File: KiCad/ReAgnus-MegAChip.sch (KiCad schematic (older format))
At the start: 24 parts, among them J3 Conn_02x01, J4 Conn_01x01, J5 Conn_01x01, J6 Conn_01x01, J7 Conn_01x01, U1 PLCC-84-Plug, U2 LM1117-3.3, U3 SN74CBTD16210, U4 SN74CBTD16210, U5 SN74CBTD16210, U6 SN74CBTD16210, U8 74LVC1G07, U9 Agnus_TH_plug_pins

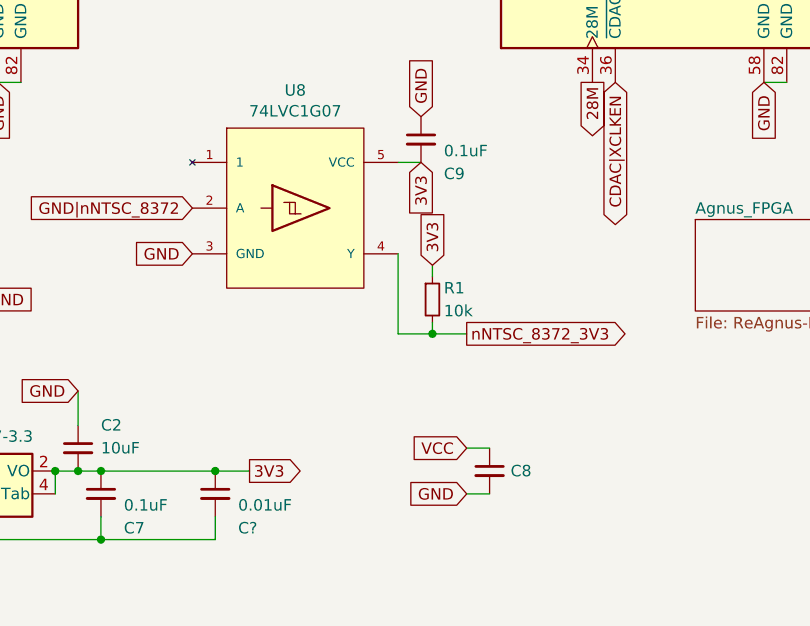
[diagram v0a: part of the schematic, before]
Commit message: fixed routing for VCC to voltage regulator, placed two-pin header for VCC/GND and more routing
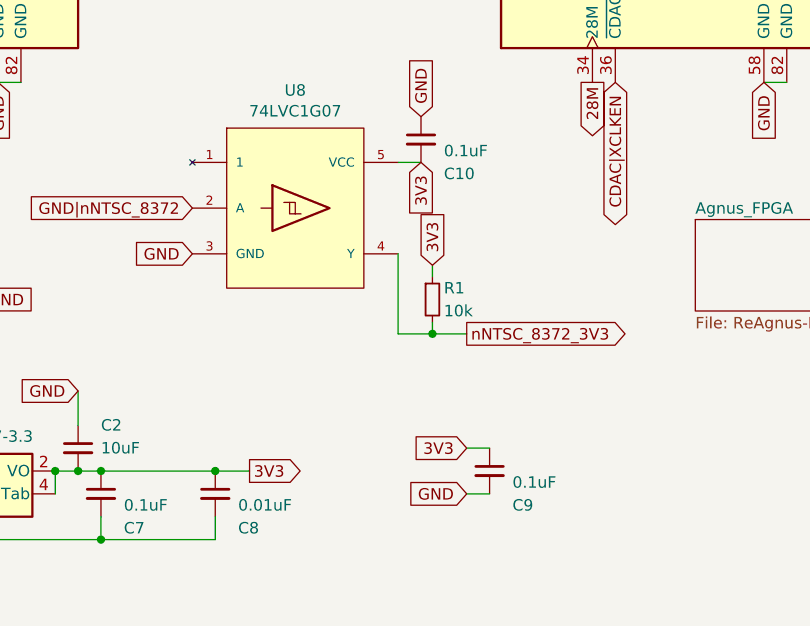
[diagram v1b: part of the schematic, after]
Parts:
- removed C8: C_Small, Capacitor_SMD:C_1210_3225Metric_Pad1.42x2.65mm_HandSolder, symbol Device:C_Small
- added C9: 0.1uF, Capacitor_SMD:C_0805_2012Metric_Pad1.15x1.40mm_HandSolder, symbol Device:C_Small
- gave numbers to parts that had none: 1
- renumbered C9 to C10
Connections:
- net 3V3: now also C9.1
- net GND: now also C9.2
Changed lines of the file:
@@
 GND
 $Comp
-L Device:C_Small C9
+L Device:C_Small C10
 U 1 1 631B6BE4
 P 4150 5950
-AR Path="/631B6BE4" Ref="C9"  Part="1"
+AR Path="/631B6BE4" Ref="C10"  Part="1"
 AR Path="/632D3BDF/631B6BE4" Ref="C?"  Part="1"
 AR Path="/632F104D/631B6BE4" Ref="C?"  Part="1"
-F 0 "C9" H 4250 5800 50  0000 L CNN
+F 0 "C10" H 4250 5800 50  0000 L CNN
 F 1 "0.1uF" H 4250 5900 50  0000 L CNN
 F 2 "Capacitor_SMD:C_0805_2012Metric_Pad1.15x1.40mm_HandSolder" H 4150 5950 50  0001 C CNN
@@
 GND|nNTSC_8372
 Connection ~ 2750 7400
-Text GLabel 4350 7300 0    50   Input ~ 0
-VCC
 Text GLabel 4350 7500 0    50   Input ~ 0
 GND
-$Comp
-L Device:C_Small C8
-U 1 1 631ACF4A
-P 4450 7400
-AR Path="/631ACF4A" Ref="C8"  Part="1"
-AR Path="/632D3BDF/631ACF4A" Ref="C?"  Part="1"
-AR Path="/632F104D/631ACF4A" Ref="C?"  Part="1"
-F 0 "C8" H 4542 7400 50  0000 L CNN
-F 1 "C_Small" H 4542 7355 50  0001 L CNN
-F 2 "Capacitor_SMD:C_1210_3225Metric_Pad1.42x2.65mm_HandSolder" H 4450 7400 50  0001 C CNN
-F 3 "~" H 4450 7400 50  0001 C CNN
-	1    4450 7400
-	1    0    0    -1
-$EndComp
 Wire Wire Line
 	4350 7300 4450 7300
@@
 	4350 7500 4450 7500
 $Comp
-L Device:C_Small C?
+L Device:C_Small C8
 U 1 1 631E37EB
 P 3250 7500
-AR Path="/631E37EB" Ref="C?"  Part="1"
+AR Path="/631E37EB" Ref="C8"  Part="1"
 AR Path="/632D3BDF/631E37EB" Ref="C?"  Part="1"
 AR Path="/632F104D/631E37EB" Ref="C?"  Part="1"
-F 0 "C?" H 3350 7350 50  0000 L CNN
+F 0 "C8" H 3350 7350 50  0000 L CNN
 F 1 "0.01uF" H 3350 7450 50  0000 L CNN
 F 2 "Capacitor_SMD:C_0603_1608Metric_Pad1.05x0.95mm_HandSolder" H 3250 7500 50  0001 C CNN
@@
 	3250 7700 3250 7600
 Connection ~ 2750 7700
+$Comp
+L Device:C_Small C9
+U 1 1 6323D0F6
+P 4450 7400
+AR Path="/6323D0F6" Ref="C9"  Part="1"
+AR Path="/632D3BDF/6323D0F6" Ref="C?"  Part="1"
+AR Path="/632F104D/6323D0F6" Ref="C?"  Part="1"
+F 0 "C9" H 4550 7250 50  0000 L CNN
+F 1 "0.1uF" H 4550 7350 50  0000 L CNN
+F 2 "Capacitor_SMD:C_0805_2012Metric_Pad1.15x1.40mm_HandSolder" H 4450 7400 50  0001 C CNN
+F 3 "~" H 4450 7400 50  0001 C CNN
+	1    4450 7400
+	1    0    0    -1
+$EndComp
+Text GLabel 4350 7300 0    50   Input ~ 0
+3V3
 $EndSCHEMATC

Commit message: more routing and placing components
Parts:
- removed R1: 10k, Resistor_SMD:R_0603_1608Metric_Pad1.05x0.95mm_HandSolder, symbol Device:R_Small
- added C11: 0.01uF, Capacitor_SMD:C_0603_1608Metric_Pad1.05x0.95mm_HandSolder, symbol Device:C_Small
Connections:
- net 3V3: now also C10.1, C11.1; no longer C10.2
- net GND: now also C10.2, C11.2; no longer C10.1
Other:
- note added: "Pulled-up in RN1 (10k)"
- moved on the sheet: C10
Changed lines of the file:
@@
 	2250 7700 2750 7700
-Wire Wire Line
-	4050 6800 4200 6800
 Wire Wire Line
 	4050 6450 4050 6800
@@
 L Device:C_Small C10
 U 1 1 631B6BE4
-P 4150 5950
+P 4650 7400
 AR Path="/631B6BE4" Ref="C10"  Part="1"
 AR Path="/632D3BDF/631B6BE4" Ref="C?"  Part="1"
 AR Path="/632F104D/631B6BE4" Ref="C?"  Part="1"
-F 0 "C10" H 4250 5800 50  0000 L CNN
-F 1 "0.1uF" H 4250 5900 50  0000 L CNN
-F 2 "Capacitor_SMD:C_0805_2012Metric_Pad1.15x1.40mm_HandSolder" H 4150 5950 50  0001 C CNN
-F 3 "~" H 4150 5950 50  0001 C CNN
-	1    4150 5950
+F 0 "C10" H 4650 7250 50  0000 L CNN
+F 1 "0.1uF" H 4650 7150 50  0000 L CNN
+F 2 "Capacitor_SMD:C_0805_2012Metric_Pad1.15x1.40mm_HandSolder" H 4650 7400 50  0001 C CNN
+F 3 "~" H 4650 7400 50  0001 C CNN
+	1    4650 7400
 	1    0    0    -1
 $EndComp
-Text GLabel 4150 6050 3    50   Input ~ 0
+Text GLabel 4050 6050 2    50   Input ~ 0
 3V3
-Wire Wire Line
-	4050 6050 4150 6050
-Text GLabel 4150 5850 1    50   Input ~ 0
-GND
 Text GLabel 8450 4800 2    50   Output ~ 0
 LDS|UDS_3V3
 Text GLabel 7450 4600 0    50   Input ~ 0
 LDS|UDS
-Text GLabel 4200 6500 1    50   Input ~ 0
-3V3
-$Comp
-L Device:R_Small R1
-U 1 1 6328BA47
-P 4200 6650
-F 0 "R1" H 4250 6700 50  0000 L CNN
-F 1 "10k" H 4250 6600 50  0000 L CNN
-F 2 "Resistor_SMD:R_0603_1608Metric_Pad1.05x0.95mm_HandSolder" H 4200 6650 50  0001 C CNN
-F 3 "~" H 4200 6650 50  0001 C CNN
-	1    4200 6650
-	1    0    0    -1
-$EndComp
-Wire Wire Line
-	4200 6500 4200 6550
-Wire Wire Line
-	4200 6750 4200 6800
-Connection ~ 4200 6800
-Wire Wire Line
-	4200 6800 4350 6800
 Text GLabel 3150 6250 0    50   Input ~ 0
 GND|nNTSC_8372
@@
 AR Path="/632D3BDF/6323D0F6" Ref="C?"  Part="1"
 AR Path="/632F104D/6323D0F6" Ref="C?"  Part="1"
-F 0 "C9" H 4550 7250 50  0000 L CNN
-F 1 "0.1uF" H 4550 7350 50  0000 L CNN
+F 0 "C9" H 4400 7250 50  0000 L CNN
+F 1 "0.1uF" H 4400 7150 50  0000 L CNN
 F 2 "Capacitor_SMD:C_0805_2012Metric_Pad1.15x1.40mm_HandSolder" H 4450 7400 50  0001 C CNN
 F 3 "~" H 4450 7400 50  0001 C CNN
@@
 Text GLabel 4350 7300 0    50   Input ~ 0
 3V3
+Wire Wire Line
+	4450 7300 4650 7300
+Connection ~ 4450 7300
+Wire Wire Line
+	4450 7500 4650 7500
+Connection ~ 4450 7500
+Text GLabel 5350 7500 0    50   Input ~ 0
+GND
+Wire Wire Line
+	5350 7300 5450 7300
+Wire Wire Line
+	5350 7500 5450 7500
+$Comp
+L Device:C_Small C11
+U 1 1 632C350C
+P 5450 7400
+AR Path="/632C350C" Ref="C11"  Part="1"
+AR Path="/632D3BDF/632C350C" Ref="C?"  Part="1"
+AR Path="/632F104D/632C350C" Ref="C?"  Part="1"
+F 0 "C11" H 5400 7250 50  0000 L CNN
+F 1 "0.01uF" H 5400 7150 50  0000 L CNN
+F 2 "Capacitor_SMD:C_0603_1608Metric_Pad1.05x0.95mm_HandSolder" H 5450 7400 50  0001 C CNN
+F 3 "~" H 5450 7400 50  0001 C CNN
+	1    5450 7400
+	1    0    0    -1
+$EndComp
+Text GLabel 5350 7300 0    50   Input ~ 0
+3V3
+Wire Wire Line
+	4050 6800 4350 6800
+Text Notes 4050 6700 0    50   ~ 0
+Pulled-up in RN1 (10k)
 $EndSCHEMATC

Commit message: more routing and placing components
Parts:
- added C11: 0.1uF, Capacitor_SMD:C_0805_2012Metric_Pad1.15x1.40mm_HandSolder, symbol Device:C_Small
- added C12, C13: 0.01uF, Capacitor_SMD:C_0805_2012Metric_Pad1.15x1.40mm_HandSolder, symbol Device:C_Small
- C3, C4, C5: value C_Small -> 0.1uF
- renumbered C11 to C15
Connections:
- wire segments 40 -> 42
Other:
- note added: "Pulled-up with RN1 (10k)"
- note removed: "Pulled-up in RN1 (10k)"
- moved on the sheet: C10, C15, C9
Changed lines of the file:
@@
 $EndComp
 $Sheet
-S 5350 6300 850  400
+S 5450 6150 850  400
 U 632F104D
 F0 "Agnus_FPGA" 50
@@
 Text GLabel 7450 1550 0    50   Output ~ 0
 7M|CDAC
-Text GLabel 4350 6800 2    50   Output ~ 0
+Text GLabel 4050 6450 2    50   Output ~ 0
 nNTSC_8372_3V3
 Text GLabel 4350 3200 0    50   BiDi ~ 0
@@
 P 9250 2450
 F 0 "C4" H 9342 2450 50  0000 L CNN
-F 1 "C_Small" H 9342 2405 50  0001 L CNN
+F 1 "0.1uF" H 9250 2550 50  0000 L CNN
 F 2 "Capacitor_SMD:C_0603_1608Metric_Pad1.05x0.95mm_HandSolder" H 9250 2450 50  0001 C CNN
 F 3 "~" H 9250 2450 50  0001 C CNN
@@
 P 7100 5300
 F 0 "C5" H 7192 5300 50  0000 L CNN
-F 1 "C_Small" H 7192 5255 50  0001 L CNN
+F 1 "0.1uF" H 7100 5450 50  0000 L CNN
 F 2 "Capacitor_SMD:C_0603_1608Metric_Pad1.05x0.95mm_HandSolder" H 7100 5300 50  0001 C CNN
 F 3 "~" H 7100 5300 50  0001 C CNN
@@
 U 1 1 6378D492
 P 7000 2450
-F 0 "C3" H 7092 2450 50  0000 L CNN
-F 1 "C_Small" H 7092 2405 50  0001 L CNN
+F 0 "C3" H 7100 2450 50  0000 L CNN
+F 1 "0.1uF" H 7000 2550 50  0000 L CNN
 F 2 "Capacitor_SMD:C_0603_1608Metric_Pad1.05x0.95mm_HandSolder" H 7000 2450 50  0001 C CNN
 F 3 "~" H 7000 2450 50  0001 C CNN
@@
 Wire Wire Line
 	2250 7700 2750 7700
-Wire Wire Line
-	4050 6450 4050 6800
 $Comp
 L ReAgnus-MegAChip:74LVC1G07 U8
@@
 L Device:C_Small C10
 U 1 1 631B6BE4
-P 4650 7400
+P 4650 7450
 AR Path="/631B6BE4" Ref="C10"  Part="1"
 AR Path="/632D3BDF/631B6BE4" Ref="C?"  Part="1"
 AR Path="/632F104D/631B6BE4" Ref="C?"  Part="1"
-F 0 "C10" H 4650 7250 50  0000 L CNN
-F 1 "0.1uF" H 4650 7150 50  0000 L CNN
-F 2 "Capacitor_SMD:C_0805_2012Metric_Pad1.15x1.40mm_HandSolder" H 4650 7400 50  0001 C CNN
-F 3 "~" H 4650 7400 50  0001 C CNN
-	1    4650 7400
+F 0 "C10" H 4650 7300 50  0000 L CNN
+F 1 "0.1uF" H 4650 7200 50  0000 L CNN
+F 2 "Capacitor_SMD:C_0805_2012Metric_Pad1.15x1.40mm_HandSolder" H 4650 7450 50  0001 C CNN
+F 3 "~" H 4650 7450 50  0001 C CNN
+	1    4650 7450
 	1    0    0    -1
 $EndComp
@@
 GND|nNTSC_8372
 Connection ~ 2750 7400
-Text GLabel 4350 7500 0    50   Input ~ 0
-GND
-Wire Wire Line
-	4350 7300 4450 7300
-Wire Wire Line
-	4350 7500 4450 7500
+Text GLabel 4300 7550 0    50   Input ~ 0
+GND
+Wire Wire Line
+	4300 7350 4400 7350
+Wire Wire Line
+	4300 7550 4400 7550
 $Comp
 L Device:C_Small C8
@@
 L Device:C_Small C9
 U 1 1 6323D0F6
-P 4450 7400
+P 4400 7450
 AR Path="/6323D0F6" Ref="C9"  Part="1"
 AR Path="/632D3BDF/6323D0F6" Ref="C?"  Part="1"
 AR Path="/632F104D/6323D0F6" Ref="C?"  Part="1"
-F 0 "C9" H 4400 7250 50  0000 L CNN
-F 1 "0.1uF" H 4400 7150 50  0000 L CNN
-F 2 "Capacitor_SMD:C_0805_2012Metric_Pad1.15x1.40mm_HandSolder" H 4450 7400 50  0001 C CNN
-F 3 "~" H 4450 7400 50  0001 C CNN
-	1    4450 7400
-	1    0    0    -1
-$EndComp
-Text GLabel 4350 7300 0    50   Input ~ 0
+F 0 "C9" H 4350 7300 50  0000 L CNN
+F 1 "0.1uF" H 4350 7200 50  0000 L CNN
+F 2 "Capacitor_SMD:C_0805_2012Metric_Pad1.15x1.40mm_HandSolder" H 4400 7450 50  0001 C CNN
+F 3 "~" H 4400 7450 50  0001 C CNN
+	1    4400 7450
+	1    0    0    -1
+$EndComp
+Text GLabel 4300 7350 0    50   Input ~ 0
 3V3
-Wire Wire Line
-	4450 7300 4650 7300
-Connection ~ 4450 7300
-Wire Wire Line
-	4450 7500 4650 7500
-Connection ~ 4450 7500
-Text GLabel 5350 7500 0    50   Input ~ 0
-GND
-Wire Wire Line
-	5350 7300 5450 7300
-Wire Wire Line
-	5350 7500 5450 7500
-$Comp
-L Device:C_Small C11
+Connection ~ 4400 7350
+Connection ~ 4400 7550
+Wire Wire Line
+	4300 6850 4400 6850
+$Comp
+L Device:C_Small C15
 U 1 1 632C350C
-P 5450 7400
-AR Path="/632C350C" Ref="C11"  Part="1"
+P 4950 6950
+AR Path="/632C350C" Ref="C15"  Part="1"
 AR Path="/632D3BDF/632C350C" Ref="C?"  Part="1"
 AR Path="/632F104D/632C350C" Ref="C?"  Part="1"
-F 0 "C11" H 5400 7250 50  0000 L CNN
-F 1 "0.01uF" H 5400 7150 50  0000 L CNN
-F 2 "Capacitor_SMD:C_0603_1608Metric_Pad1.05x0.95mm_HandSolder" H 5450 7400 50  0001 C CNN
-F 3 "~" H 5450 7400 50  0001 C CNN
-	1    5450 7400
-	1    0    0    -1
-$EndComp
-Text GLabel 5350 7300 0    50   Input ~ 0
+F 0 "C15" H 4900 6800 50  0000 L CNN
+F 1 "0.01uF" H 4900 6700 50  0000 L CNN
+F 2 "Capacitor_SMD:C_0603_1608Metric_Pad1.05x0.95mm_HandSolder" H 4950 6950 50  0001 C CNN
+F 3 "~" H 4950 6950 50  0001 C CNN
+	1    4950 6950
+	1    0    0    -1
+$EndComp
+Text GLabel 4300 6850 0    50   Input ~ 0
 3V3
-Wire Wire Line
-	4050 6800 4350 6800
-Text Notes 4050 6700 0    50   ~ 0
-Pulled-up in RN1 (10k)
+Text Notes 4050 6600 0    50   ~ 0
+Pulled-up with RN1 (10k)
+$Comp
+L Device:C_Small C11
+U 1 1 63302CD2
+P 4900 7450
+AR Path="/63302CD2" Ref="C11"  Part="1"
+AR Path="/632D3BDF/63302CD2" Ref="C?"  Part="1"
+AR Path="/632F104D/63302CD2" Ref="C?"  Part="1"
+F 0 "C11" H 4900 7300 50  0000 L CNN
+F 1 "0.1uF" H 4900 7200 50  0000 L CNN
+F 2 "Capacitor_SMD:C_0805_2012Metric_Pad1.15x1.40mm_HandSolder" H 4900 7450 50  0001 C CNN
+F 3 "~" H 4900 7450 50  0001 C CNN
+	1    4900 7450
+	1    0    0    -1
+$EndComp
+Connection ~ 4650 7350
+Connection ~ 4650 7550
+Connection ~ 4900 7350
+Connection ~ 4900 7550
+Wire Wire Line
+	4400 7350 4650 7350
+Wire Wire Line
+	4400 7550 4650 7550
+Wire Wire Line
+	4650 7350 4900 7350
+Wire Wire Line
+	4650 7550 4900 7550
+$Comp
+L Device:C_Small C13
+U 1 1 6333CF1B
+P 4650 6950
+AR Path="/6333CF1B" Ref="C13"  Part="1"
+AR Path="/632D3BDF/6333CF1B" Ref="C?"  Part="1"
+AR Path="/632F104D/6333CF1B" Ref="C?"  Part="1"
+F 0 "C13" H 4600 6800 50  0000 L CNN
+F 1 "0.01uF" H 4600 6700 50  0000 L CNN
+F 2 "Capacitor_SMD:C_0805_2012Metric_Pad1.15x1.40mm_HandSolder" H 4650 6950 50  0001 C CNN
+F 3 "~" H 4650 6950 50  0001 C CNN
+	1    4650 6950
+	1    0    0    -1
+$EndComp
+Wire Wire Line
+	4900 7350 5400 7350
+Wire Wire Line
+	4900 7550 5400 7550
+$Comp
+L Device:C_Small C12
+U 1 1 633036BF
+P 4400 6950
+AR Path="/633036BF" Ref="C12"  Part="1"
+AR Path="/632D3BDF/633036BF" Ref="C?"  Part="1"
+AR Path="/632F104D/633036BF" Ref="C?"  Part="1"
+F 0 "C12" H 4300 6800 50  0000 L CNN
+F 1 "0.01uF" H 4300 6700 50  0000 L CNN
+F 2 "Capacitor_SMD:C_0805_2012Metric_Pad1.15x1.40mm_HandSolder" H 4400 6950 50  0001 C CNN
+F 3 "~" H 4400 6950 50  0001 C CNN
+	1    4400 6950
+	1    0    0    -1
+$EndComp
+Wire Wire Line
+	4300 7050 4400 7050
+Text GLabel 4300 7050 0    50   Input ~ 0
+GND
 $EndSCHEMATC

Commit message: more routing and placing components
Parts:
- added C12: 0.1uF, Capacitor_SMD:C_0805_2012Metric_Pad1.15x1.40mm_HandSolder, symbol Device:C_Small
- added C16: CP_Small, Capacitor_THT:CP_Radial_D5.0mm_P2.50mm, symbol Device:CP_Small
- renumbered C12 to C13, C13 to C14
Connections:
- wire segments 42 -> 48
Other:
- moved on the sheet: C14, C15
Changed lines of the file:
@@
 L Device:C_Small C15
 U 1 1 632C350C
-P 4950 6950
+P 4800 6950
 AR Path="/632C350C" Ref="C15"  Part="1"
 AR Path="/632D3BDF/632C350C" Ref="C?"  Part="1"
 AR Path="/632F104D/632C350C" Ref="C?"  Part="1"
-F 0 "C15" H 4900 6800 50  0000 L CNN
-F 1 "0.01uF" H 4900 6700 50  0000 L CNN
-F 2 "Capacitor_SMD:C_0603_1608Metric_Pad1.05x0.95mm_HandSolder" H 4950 6950 50  0001 C CNN
-F 3 "~" H 4950 6950 50  0001 C CNN
-	1    4950 6950
+F 0 "C15" H 4750 6800 50  0000 L CNN
+F 1 "0.01uF" H 4750 6700 50  0001 L CNN
+F 2 "Capacitor_SMD:C_0603_1608Metric_Pad1.05x0.95mm_HandSolder" H 4800 6950 50  0001 C CNN
+F 3 "~" H 4800 6950 50  0001 C CNN
+	1    4800 6950
 	1    0    0    -1
 $EndComp
@@
 	4650 7550 4900 7550
 $Comp
-L Device:C_Small C13
+L Device:C_Small C14
 U 1 1 6333CF1B
-P 4650 6950
-AR Path="/6333CF1B" Ref="C13"  Part="1"
+P 4600 6950
+AR Path="/6333CF1B" Ref="C14"  Part="1"
 AR Path="/632D3BDF/6333CF1B" Ref="C?"  Part="1"
 AR Path="/632F104D/6333CF1B" Ref="C?"  Part="1"
-F 0 "C13" H 4600 6800 50  0000 L CNN
-F 1 "0.01uF" H 4600 6700 50  0000 L CNN
-F 2 "Capacitor_SMD:C_0805_2012Metric_Pad1.15x1.40mm_HandSolder" H 4650 6950 50  0001 C CNN
-F 3 "~" H 4650 6950 50  0001 C CNN
-	1    4650 6950
+F 0 "C14" H 4550 6800 50  0000 L CNN
+F 1 "0.01uF" H 4550 6700 50  0001 L CNN
+F 2 "Capacitor_SMD:C_0805_2012Metric_Pad1.15x1.40mm_HandSolder" H 4600 6950 50  0001 C CNN
+F 3 "~" H 4600 6950 50  0001 C CNN
+	1    4600 6950
 	1    0    0    -1
 $EndComp
 Wire Wire Line
-	4900 7350 5400 7350
+	4900 7350 5150 7350
 Wire Wire Line
-	4900 7550 5400 7550
+	4900 7550 5150 7550
 $Comp
-L Device:C_Small C12
+L Device:C_Small C13
 U 1 1 633036BF
 P 4400 6950
-AR Path="/633036BF" Ref="C12"  Part="1"
+AR Path="/633036BF" Ref="C13"  Part="1"
 AR Path="/632D3BDF/633036BF" Ref="C?"  Part="1"
 AR Path="/632F104D/633036BF" Ref="C?"  Part="1"
-F 0 "C12" H 4300 6800 50  0000 L CNN
-F 1 "0.01uF" H 4300 6700 50  0000 L CNN
+F 0 "C13" H 4300 6800 50  0000 L CNN
+F 1 "0.01uF" H 4300 6700 50  0001 L CNN
 F 2 "Capacitor_SMD:C_0805_2012Metric_Pad1.15x1.40mm_HandSolder" H 4400 6950 50  0001 C CNN
 F 3 "~" H 4400 6950 50  0001 C CNN
@@
 Text GLabel 4300 7050 0    50   Input ~ 0
 GND
+$Comp
+L Device:C_Small C12
+U 1 1 6335E2C8
+P 5150 7450
+AR Path="/6335E2C8" Ref="C12"  Part="1"
+AR Path="/632D3BDF/6335E2C8" Ref="C?"  Part="1"
+AR Path="/632F104D/6335E2C8" Ref="C?"  Part="1"
+F 0 "C12" H 5150 7300 50  0000 L CNN
+F 1 "0.1uF" H 5150 7200 50  0000 L CNN
+F 2 "Capacitor_SMD:C_0805_2012Metric_Pad1.15x1.40mm_HandSolder" H 5150 7450 50  0001 C CNN
+F 3 "~" H 5150 7450 50  0001 C CNN
+	1    5150 7450
+	1    0    0    -1
+$EndComp
+Connection ~ 5150 7350
+Wire Wire Line
+	5150 7350 5400 7350
+Connection ~ 5150 7550
+Wire Wire Line
+	5150 7550 5400 7550
+$Comp
+L Device:CP_Small C16
+U 1 1 63371DE3
+P 3150 6950
+F 0 "C16" H 3238 6996 50  0000 L CNN
+F 1 "CP_Small" H 3238 6905 50  0000 L CNN
+F 2 "Capacitor_THT:CP_Radial_D5.0mm_P2.50mm" H 3150 6950 50  0001 C CNN
+F 3 "~" H 3150 6950 50  0001 C CNN
+	1    3150 6950
+	1    0    0    -1
+$EndComp
+Wire Wire Line
+	4400 6850 4600 6850
+Connection ~ 4400 6850
+Wire Wire Line
+	4400 7050 4600 7050
+Connection ~ 4400 7050
+Connection ~ 4600 6850
+Connection ~ 4600 7050
+Wire Wire Line
+	4600 6850 4800 6850
+Wire Wire Line
+	4600 7050 4800 7050
+Text GLabel 3150 7050 3    50   Input ~ 0
+GND
+Text GLabel 3150 6850 1    50   Input ~ 0
+VCC
 $EndSCHEMATC
